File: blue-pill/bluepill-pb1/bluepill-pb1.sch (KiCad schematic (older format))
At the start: 31 parts, among them J1 pc850vs_11_pin, J2 Conn_01x04, J3 Conn_01x04, J4 Conn_01x04, J5 Conn_01x09, J6 Conn_01x06, J7 Conn_01x02, Q1 Q_NPN_CBE, SW1 Switch_SW_SPST, SW2 Switch_SW_SPST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

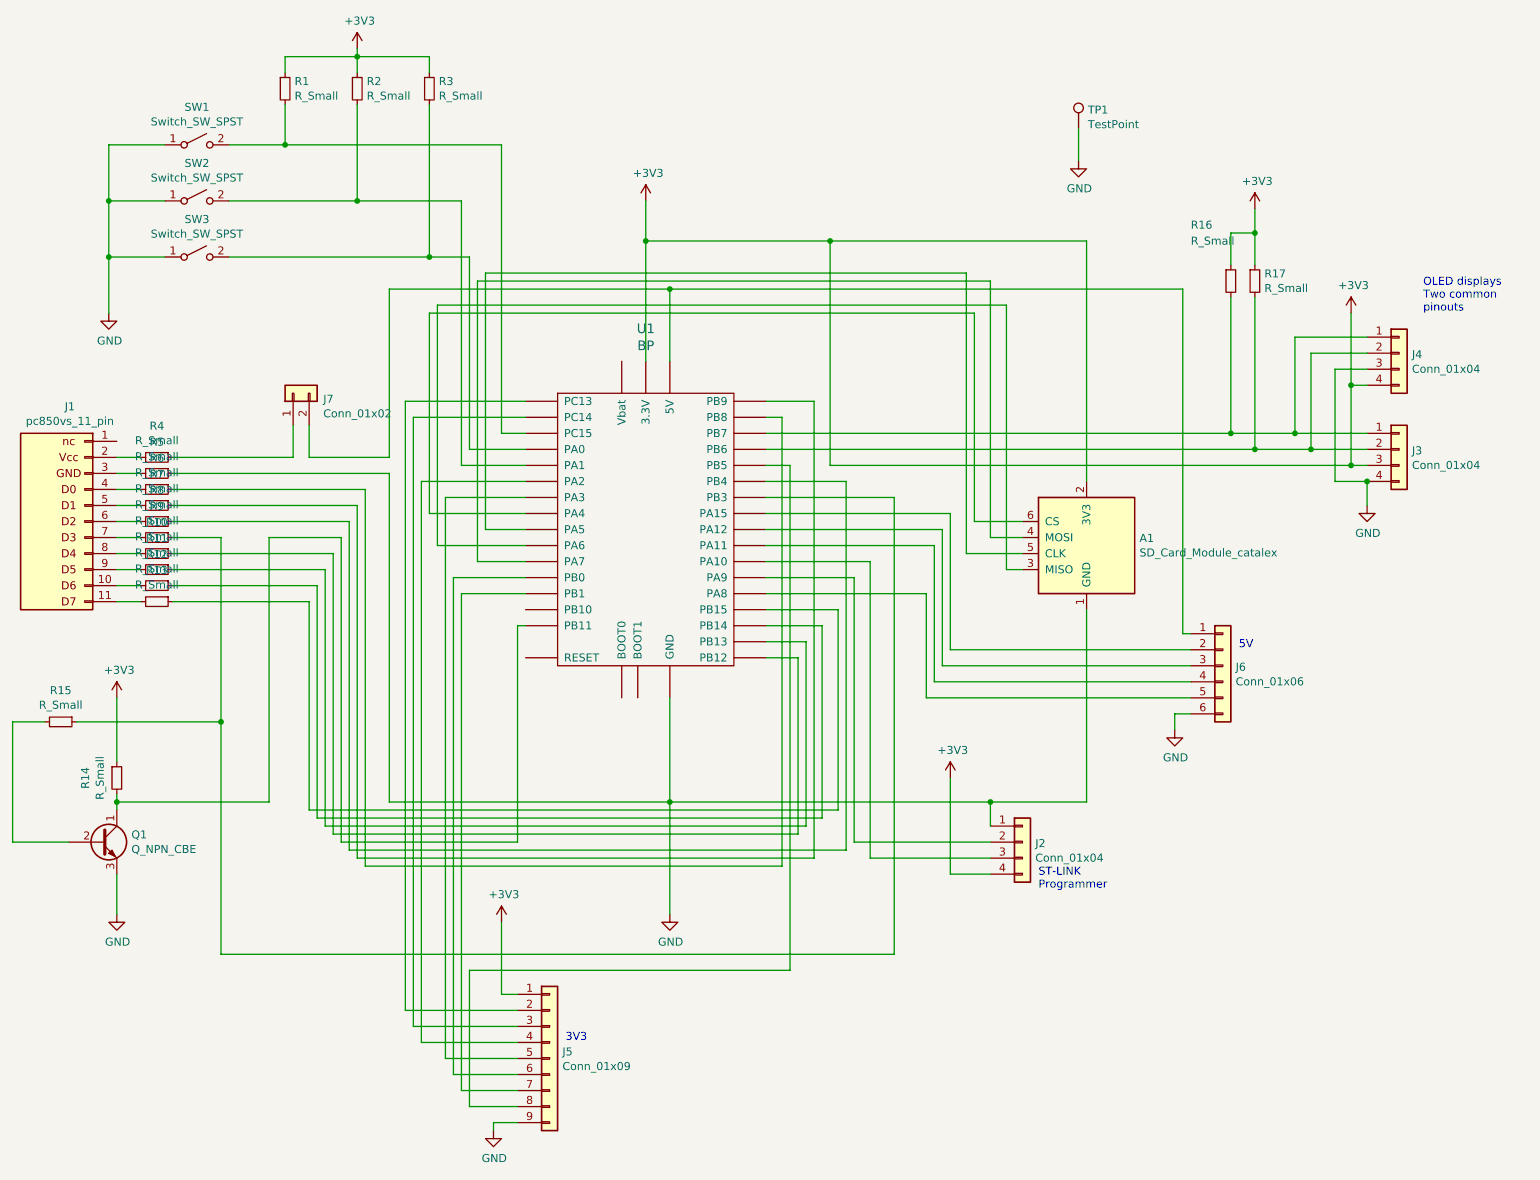
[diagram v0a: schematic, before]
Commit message: Added component values
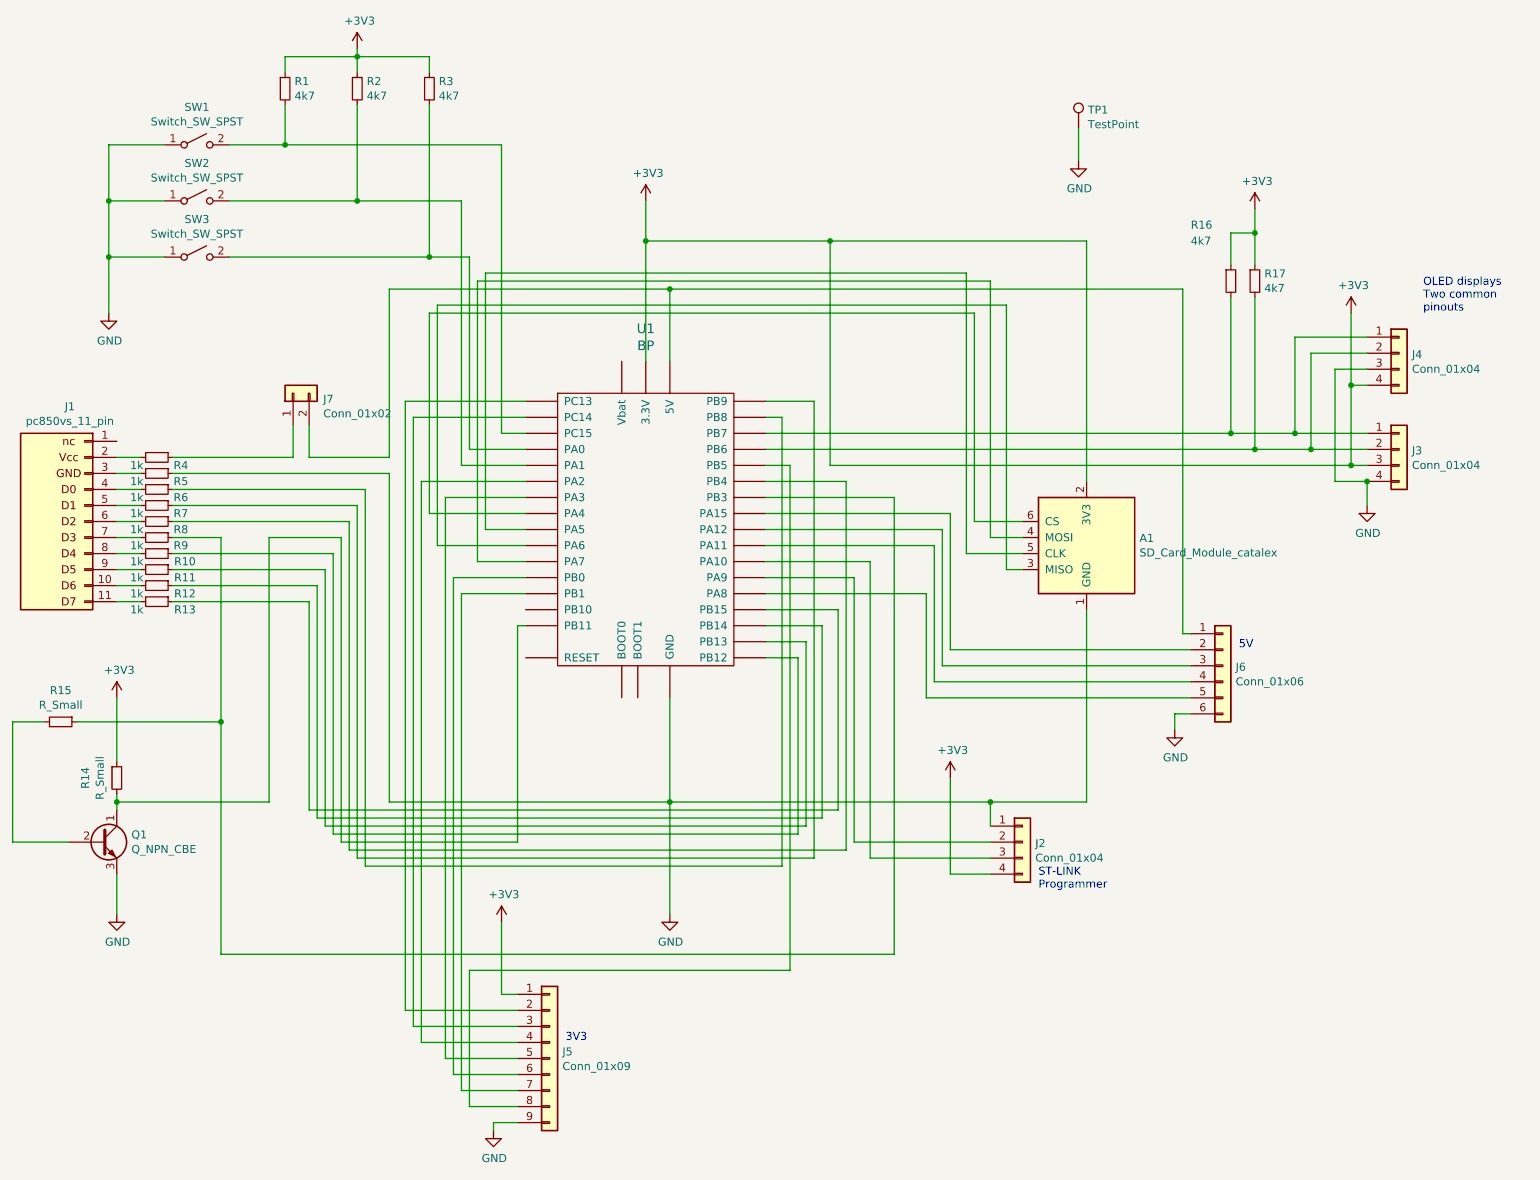
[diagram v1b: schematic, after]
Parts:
- R1, R16, R17, R2, R3: value R_Small -> 4k7
- R10, R11, R12, R13, R4, R5, R6, R7, R8, R9: value R_Small -> 1k
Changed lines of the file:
@@
 P 2700 1000
 F 0 "R1" H 2759 1046 50  0000 L CNN
-F 1 "R_Small" H 2759 955 50  0000 L CNN
+F 1 "4k7" H 2759 955 50  0000 L CNN
 F 2 "Resistor_THT:R_Axial_DIN0207_L6.3mm_D2.5mm_P7.62mm_Horizontal" H 2700 1000 50  0001 C CNN
 F 3 "~" H 2700 1000 50  0001 C CNN
@@
 P 3150 1000
 F 0 "R2" H 3209 1046 50  0000 L CNN
-F 1 "R_Small" H 3209 955 50  0000 L CNN
+F 1 "4k7" H 3209 955 50  0000 L CNN
 F 2 "Resistor_THT:R_Axial_DIN0207_L6.3mm_D2.5mm_P7.62mm_Horizontal" H 3150 1000 50  0001 C CNN
 F 3 "~" H 3150 1000 50  0001 C CNN
@@
 P 3600 1000
 F 0 "R3" H 3659 1046 50  0000 L CNN
-F 1 "R_Small" H 3659 955 50  0000 L CNN
+F 1 "4k7" H 3659 955 50  0000 L CNN
 F 2 "Resistor_THT:R_Axial_DIN0207_L6.3mm_D2.5mm_P7.62mm_Horizontal" H 3600 1000 50  0001 C CNN
 F 3 "~" H 3600 1000 50  0001 C CNN
@@
 U 1 1 5F05AB58
 P 1900 3300
-F 0 "R4" V 1704 3300 50  0000 C CNN
-F 1 "R_Small" V 1795 3300 50  0000 C CNN
+F 0 "R4" V 1950 3450 50  0000 C CNN
+F 1 "1k" V 1950 3175 50  0000 C CNN
 F 2 "Resistor_THT:R_Axial_DIN0207_L6.3mm_D2.5mm_P7.62mm_Horizontal" H 1900 3300 50  0001 C CNN
 F 3 "~" H 1900 3300 50  0001 C CNN
@@
 U 1 1 5F05DF15
 P 1900 3400
-F 0 "R5" V 1704 3400 50  0000 C CNN
-F 1 "R_Small" V 1795 3400 50  0000 C CNN
+F 0 "R5" V 1950 3550 50  0000 C CNN
+F 1 "1k" V 1950 3275 50  0000 C CNN
 F 2 "Resistor_THT:R_Axial_DIN0207_L6.3mm_D2.5mm_P7.62mm_Horizontal" H 1900 3400 50  0001 C CNN
 F 3 "~" H 1900 3400 50  0001 C CNN
@@
 U 1 1 5F0612A9
 P 1900 3500
-F 0 "R6" V 1704 3500 50  0000 C CNN
-F 1 "R_Small" V 1795 3500 50  0000 C CNN
+F 0 "R6" V 1950 3650 50  0000 C CNN
+F 1 "1k" V 1950 3375 50  0000 C CNN
 F 2 "Resistor_THT:R_Axial_DIN0207_L6.3mm_D2.5mm_P7.62mm_Horizontal" H 1900 3500 50  0001 C CNN
 F 3 "~" H 1900 3500 50  0001 C CNN
@@
 U 1 1 5F0646DA
 P 1900 3600
-F 0 "R7" V 1704 3600 50  0000 C CNN
-F 1 "R_Small" V 1795 3600 50  0000 C CNN
+F 0 "R7" V 1950 3750 50  0000 C CNN
+F 1 "1k" V 1950 3475 50  0000 C CNN
 F 2 "Resistor_THT:R_Axial_DIN0207_L6.3mm_D2.5mm_P7.62mm_Horizontal" H 1900 3600 50  0001 C CNN
 F 3 "~" H 1900 3600 50  0001 C CNN
@@
 U 1 1 5F067A97
 P 1900 3700
-F 0 "R8" V 1704 3700 50  0000 C CNN
-F 1 "R_Small" V 1795 3700 50  0000 C CNN
+F 0 "R8" V 1950 3850 50  0000 C CNN
+F 1 "1k" V 1950 3575 50  0000 C CNN
 F 2 "Resistor_THT:R_Axial_DIN0207_L6.3mm_D2.5mm_P7.62mm_Horizontal" H 1900 3700 50  0001 C CNN
 F 3 "~" H 1900 3700 50  0001 C CNN
@@
 U 1 1 5F06AED2
 P 1900 3800
-F 0 "R9" V 1704 3800 50  0000 C CNN
-F 1 "R_Small" V 1795 3800 50  0000 C CNN
+F 0 "R9" V 1950 3950 50  0000 C CNN
+F 1 "1k" V 1950 3675 50  0000 C CNN
 F 2 "Resistor_THT:R_Axial_DIN0207_L6.3mm_D2.5mm_P7.62mm_Horizontal" H 1900 3800 50  0001 C CNN
 F 3 "~" H 1900 3800 50  0001 C CNN
@@
 U 1 1 5F06E32C
 P 1900 3900
-F 0 "R10" V 1704 3900 50  0000 C CNN
-F 1 "R_Small" V 1795 3900 50  0000 C CNN
+F 0 "R10" V 1950 4075 50  0000 C CNN
+F 1 "1k" V 1950 3775 50  0000 C CNN
 F 2 "Resistor_THT:R_Axial_DIN0207_L6.3mm_D2.5mm_P7.62mm_Horizontal" H 1900 3900 50  0001 C CNN
 F 3 "~" H 1900 3900 50  0001 C CNN
@@
 U 1 1 5F071750
 P 1900 4000
-F 0 "R11" V 1704 4000 50  0000 C CNN
-F 1 "R_Small" V 1795 4000 50  0000 C CNN
+F 0 "R11" V 1950 4175 50  0000 C CNN
+F 1 "1k" V 1950 3875 50  0000 C CNN
 F 2 "Resistor_THT:R_Axial_DIN0207_L6.3mm_D2.5mm_P7.62mm_Horizontal" H 1900 4000 50  0001 C CNN
 F 3 "~" H 1900 4000 50  0001 C CNN
@@
 U 1 1 5F074B61
 P 1900 4100
-F 0 "R12" V 1704 4100 50  0000 C CNN
-F 1 "R_Small" V 1795 4100 50  0000 C CNN
+F 0 "R12" V 1950 4275 50  0000 C CNN
+F 1 "1k" V 1950 3975 50  0000 C CNN
 F 2 "Resistor_THT:R_Axial_DIN0207_L6.3mm_D2.5mm_P7.62mm_Horizontal" H 1900 4100 50  0001 C CNN
 F 3 "~" H 1900 4100 50  0001 C CNN
@@
 U 1 1 5F078053
 P 1900 4200
-F 0 "R13" V 1704 4200 50  0000 C CNN
-F 1 "R_Small" V 1795 4200 50  0000 C CNN
+F 0 "R13" V 1950 4375 50  0000 C CNN
+F 1 "1k" V 1950 4075 50  0000 C CNN
 F 2 "Resistor_THT:R_Axial_DIN0207_L6.3mm_D2.5mm_P7.62mm_Horizontal" H 1900 4200 50  0001 C CNN
 F 3 "~" H 1900 4200 50  0001 C CNN
@@
 P 8600 2200
 F 0 "R16" H 8350 2550 50  0000 L CNN
-F 1 "R_Small" H 8350 2450 50  0000 L CNN
+F 1 "4k7" H 8350 2450 50  0000 L CNN
 F 2 "Resistor_THT:R_Axial_DIN0207_L6.3mm_D2.5mm_P7.62mm_Horizontal" H 8600 2200 50  0001 C CNN
 F 3 "~" H 8600 2200 50  0001 C CNN
@@
 P 8750 2200
 F 0 "R17" H 8809 2246 50  0000 L CNN
-F 1 "R_Small" H 8809 2155 50  0000 L CNN
+F 1 "4k7" H 8809 2155 50  0000 L CNN
 F 2 "Resistor_THT:R_Axial_DIN0207_L6.3mm_D2.5mm_P7.62mm_Horizontal" H 8750 2200 50  0001 C CNN
 F 3 "~" H 8750 2200 50  0001 C CNN

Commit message: Fix to issue #2
The SD card would sometimes not initialise. A possible fix to this is in this
commit.
By putting a finger on various terminals I found that the CS pin of the SD card adapter
could stop initialisation of the card if it was held high. Holding it low with a high-ish
resistance allowed the SD card to initialise every time. With the theory that the CS line
was activating before or during the SD card initialisation and messing it up, holding it low with a resistor
would deselect it unless the blue pill drove the GPIO high when it wanted ot send a command
or data.
As a test, I have added an explicit GPIO output data direction setup and drive the GPIo to 0 as early
as possible. This does seem to have solved the problem I saw, which hopefully is the problem
seen everywhere.
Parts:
- R14, R15: value R_Small -> Do not fit
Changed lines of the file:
@@
 P 1650 5300
 F 0 "R14" V 1454 5300 50  0000 C CNN
-F 1 "R_Small" V 1545 5300 50  0000 C CNN
+F 1 "Do not fit" V 1545 5300 50  0000 C CNN
 F 2 "Resistor_THT:R_Axial_DIN0207_L6.3mm_D2.5mm_P7.62mm_Horizontal" H 1650 5300 50  0001 C CNN
 F 3 "~" H 1650 5300 50  0001 C CNN
@@
 P 1300 4950
 F 0 "R15" V 1104 4950 50  0000 C CNN
-F 1 "R_Small" V 1195 4950 50  0000 C CNN
+F 1 "Do not fit" V 1195 4950 50  0000 C CNN
 F 2 "Resistor_THT:R_Axial_DIN0207_L6.3mm_D2.5mm_P7.62mm_Horizontal" H 1300 4950 50  0001 C CNN
 F 3 "~" H 1300 4950 50  0001 C CNN

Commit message: Updates
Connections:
- net +3V3: no longer A1.2 (3V3)
- net at J6.1 (Pin_1), J7.2 (Pin_2), U1.5V: now also A1.2 (3V3)
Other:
- note added: "5V power to SD card, not all modules\ncan run off 3V3"
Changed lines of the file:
@@
 encoding utf-8
 Sheet 1 1
-Title ""
-Date ""
-Rev ""
+Title "PCG-850VS SD card Gadget"
+Date "2022-09-12"
+Rev "V2.2"
 Comp ""
 Comment1 ""
@@
 	3350 2250 5100 2250
 Wire Wire Line
-	5100 2250 5100 2700
+	5100 2250 5100 2650
 Wire Wire Line
 	5100 4800 5100 5450
@@
 Connection ~ 7100 5450
 Wire Wire Line
-	7700 3450 7700 1950
-Wire Wire Line
-	7700 1950 6100 1950
-Wire Wire Line
 	4950 1950 4950 2700
 $Comp
@@
 Wire Wire Line
 	6100 3350 6100 1950
-Connection ~ 6100 1950
 Wire Wire Line
 	6100 1950 4950 1950
@@
 Wire Wire Line
 	8300 2250 8300 4400
+Wire Wire Line
+	5100 2650 7700 2650
+Wire Wire Line
+	7700 2650 7700 3450
+Connection ~ 5100 2650
+Wire Wire Line
+	5100 2650 5100 2700
+Text Notes 8450 4175 0    50   ~ 0
+5V power to SD card, not all modules\ncan run off 3V3
 $EndSCHEMATC
